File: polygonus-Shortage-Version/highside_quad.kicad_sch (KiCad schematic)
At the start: 11 parts, among them U1102 BTS4175SGA, U1103 BTS4175SGA

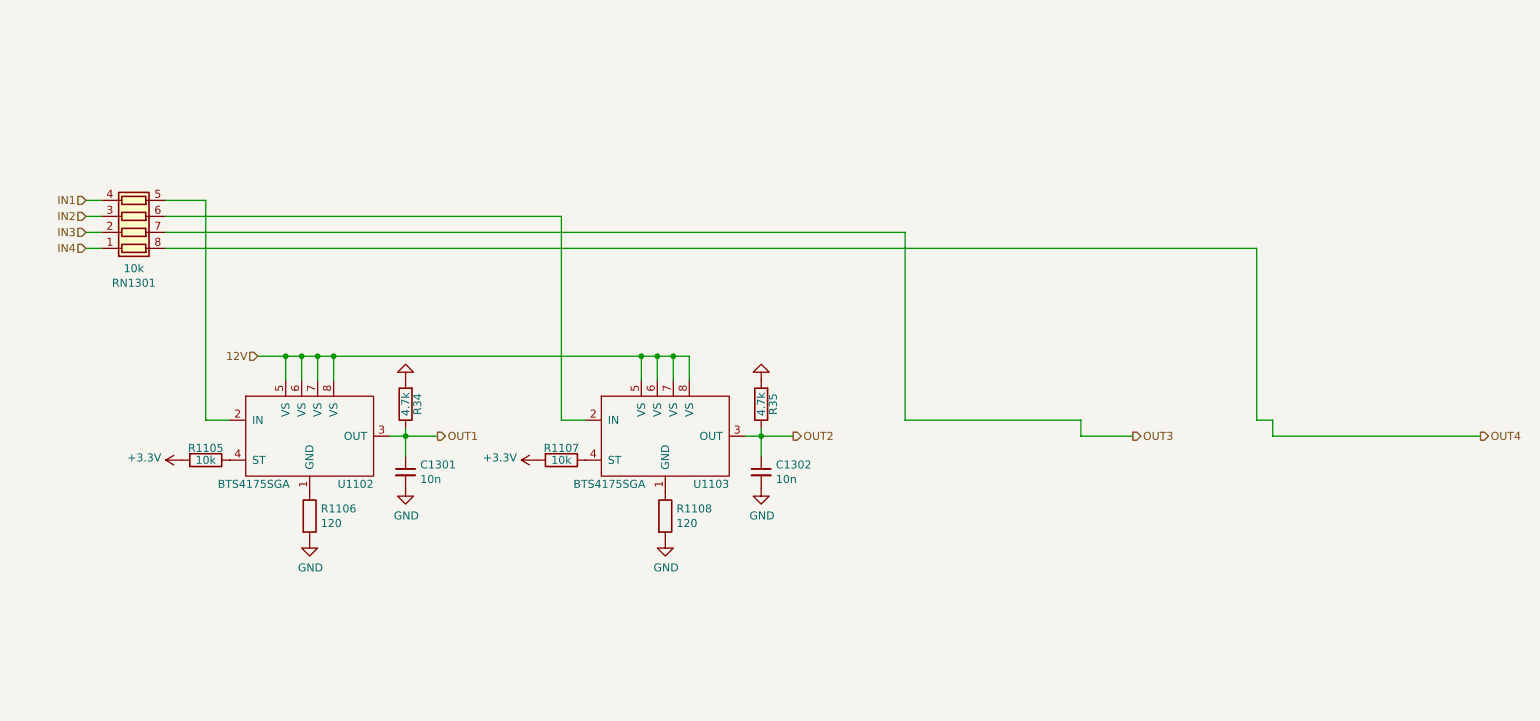
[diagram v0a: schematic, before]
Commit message: Switched highsides, changed TC4427 footprint, swapped USB to other side
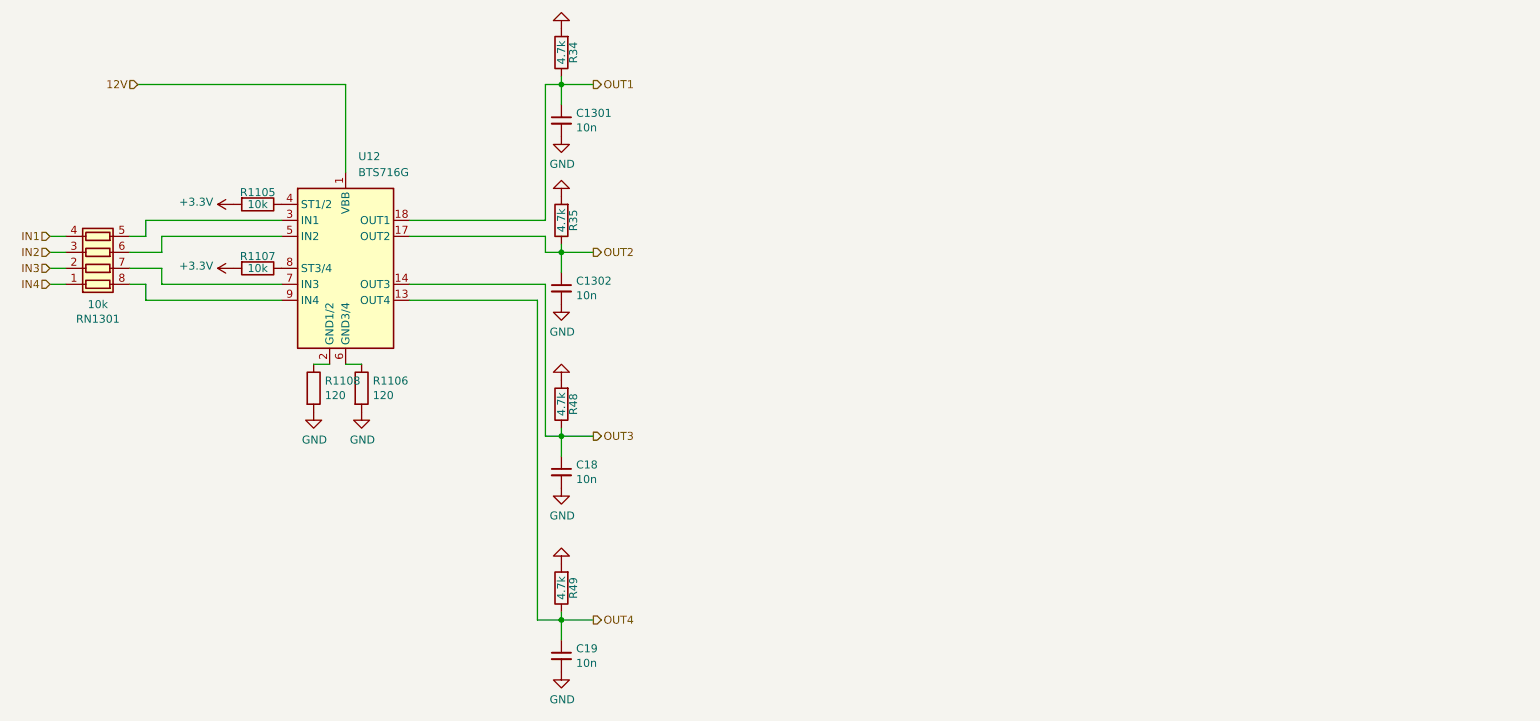
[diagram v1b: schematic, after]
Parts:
- removed U1102, U1103: BTS4175SGA, Package_SO:SOIC-8_3.9x4.9mm_P1.27mm, symbol bts4175:BTS4175SGA
- added C18, C19: 10n, Capacitor_SMD:C_0603_1608Metric, symbol Device:C_Small
- added R48, R49: 4.7k, Resistor_SMD:R_0805_2012Metric, symbol Device:R
- added U12: BTS716G, Package_SO:Infineon_PG-DSO-20-32, symbol Power_Management:BTS716G
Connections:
- net 12V: now also U12.1 (VBB), U12.10 (VBB), U12.11 (VBB), U12.12 (VBB), U12.15 (VBB), U12.16 (VBB), U12.19 (VBB), U12.20 (VBB)
- net GND: now also C18.2, C19.2, R48.2, R49.2
- net OUT1: now also U12.18 (OUT1)
- net OUT2: now also U12.17 (OUT2)
- net OUT3: now also C18.1, R48.1, U12.14 (OUT3); no longer RN1301.7 (R2.2)
- net OUT4: now also C19.1, R49.1, U12.13 (OUT4); no longer RN1301.8 (R1.2)
- net at RN1301.5 (R4.2): now also U12.3 (IN1)
- net at RN1301.6 (R3.2): now also U12.5 (IN2)
- net at R1106.1: now also U12.6 (GND3/4)
- net at R1105.1: now also U12.4 (ST1/2)
- net at R1108.1: now also U12.2 (GND1/2)
- net at R1107.1: now also U12.8 (ST3/4)
- new net: RN1301.7 (R2.2), U12.7 (IN3)
- new net: RN1301.8 (R1.2), U12.9 (IN4)
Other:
- moved on the sheet: C1301, C1302, R1105, R1106, R1107, R1108, R34, R35, RN1301

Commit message: clearout basic version
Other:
- company: rusEFI -> (none)
- title: rusEfi Proteus -> Polygonus
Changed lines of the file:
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@@
   (paper "A4")
   (title_block
-    (title "rusEfi Proteus")
-    (date "2022-04-09")
+    (title "Polygonus")
+    (date "2023-03-15")
     (rev "v0.7")
-    (company "rusEFI")
-    (comment 1 "github.com/mck1117/proteus")
     (comment 2 "rusefi.com/s/proteus")
   )

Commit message: Update to V1.3
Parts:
- renumbered C1301 to C85, C1302 to C86, C18 to C87, C19 to C88, R1107 to R100, R1108 to R101, R1106 to R102, R34 to R103, R35 to R104, R48 to R105, R49 to R106, R1105 to R99, RN1301 to RN11, U12 to U40
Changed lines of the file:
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@@
   (symbol (lib_id "Device:R_Pack04") (at 27.94 68.58 270) (mirror x) (unit 1)
     (in_bom yes) (on_board yes)
-    (property "Reference" "RN1301" (id 0) (at 27.94 79.1718 90))
+    (property "Reference" "RN11" (id 0) (at 27.94 79.1718 90))
     (property "Value" "10k" (id 1) (at 27.94 76.8604 90))
     (property "Footprint" "Resistor_SMD:R_Array_Convex_4x0603" (id 2) (at 27.94 61.595 90)
@@
   (symbol (lib_id "Device:C_Small") (at 101.6 47.625 0) (unit 1)
     (in_bom yes) (on_board yes)
-    (property "Reference" "C1301" (id 0) (at 103.9368 46.4566 0)
+    (property "Reference" "C85" (id 0) (at 103.9368 46.4566 0)
       (effects (font (size 1.27 1.27)) (justify left))
     )
@@
   (symbol (lib_id "Device:C_Small") (at 101.6 74.295 0) (unit 1)
     (in_bom yes) (on_board yes)
-    (property "Reference" "C1302" (id 0) (at 103.9368 73.1266 0)
+    (property "Reference" "C86" (id 0) (at 103.9368 73.1266 0)
       (effects (font (size 1.27 1.27)) (justify left))
     )
@@
   (symbol (lib_id "power:GND") (at 69.85 93.98 0) (unit 1)
     (in_bom yes) (on_board yes)
-    (property "Reference" "#PWR0291" (id 0) (at 69.85 100.33 0)
+    (property "Reference" "#PWR0248" (id 0) (at 69.85 100.33 0)
       (effects (font (size 1.27 1.27)) hide)
     )
@@
   (symbol (lib_id "power:GND") (at 101.6 50.165 0) (unit 1)
     (in_bom yes) (on_board yes)
-    (property "Reference" "#PWR0292" (id 0) (at 101.6 56.515 0)
+    (property "Reference" "#PWR0250" (id 0) (at 101.6 56.515 0)
       (effects (font (size 1.27 1.27)) hide)
     )
@@
   (symbol (lib_id "Device:R") (at 69.85 90.17 0) (unit 1)
     (in_bom yes) (on_board yes)
-    (property "Reference" "R1106" (id 0) (at 71.628 89.0016 0)
+    (property "Reference" "R102" (id 0) (at 71.628 89.0016 0)
       (effects (font (size 1.27 1.27)) (justify left))
     )
@@
   (symbol (lib_id "Device:R") (at 53.34 60.96 270) (unit 1)
     (in_bom yes) (on_board yes)
-    (property "Reference" "R1105" (id 0) (at 53.34 59.055 90))
+    (property "Reference" "R99" (id 0) (at 53.34 59.055 90))
     (property "Value" "10k" (id 1) (at 53.34 60.96 90))
     (property "Footprint" "Resistor_SMD:R_0402_1005Metric" (id 2) (at 53.34 59.182 90)
@@
   (symbol (lib_id "power:+3.3V") (at 49.53 60.96 90) (unit 1)
     (in_bom yes) (on_board yes)
-    (property "Reference" "#PWR0293" (id 0) (at 53.34 60.96 0)
+    (property "Reference" "#PWR0245" (id 0) (at 53.34 60.96 0)
       (effects (font (size 1.27 1.27)) hide)
     )
@@
   (symbol (lib_id "power:GND") (at 62.23 93.98 0) (unit 1)
     (in_bom yes) (on_board yes)
-    (property "Reference" "#PWR0294" (id 0) (at 62.23 100.33 0)
+    (property "Reference" "#PWR0247" (id 0) (at 62.23 100.33 0)
       (effects (font (size 1.27 1.27)) hide)
     )
@@
   (symbol (lib_id "power:GND") (at 101.6 76.835 0) (unit 1)
     (in_bom yes) (on_board yes)
-    (property "Reference" "#PWR0295" (id 0) (at 101.6 83.185 0)
+    (property "Reference" "#PWR0252" (id 0) (at 101.6 83.185 0)
       (effects (font (size 1.27 1.27)) hide)
     )
@@
   (symbol (lib_id "Device:R") (at 62.23 90.17 0) (unit 1)
     (in_bom yes) (on_board yes)
-    (property "Reference" "R1108" (id 0) (at 64.008 89.0016 0)
+    (property "Reference" "R101" (id 0) (at 64.008 89.0016 0)
       (effects (font (size 1.27 1.27)) (justify left))
     )
@@
   (symbol (lib_id "Device:R") (at 53.34 71.12 270) (unit 1)
     (in_bom yes) (on_board yes)
-    (property "Reference" "R1107" (id 0) (at 53.34 69.215 90))
+    (property "Reference" "R100" (id 0) (at 53.34 69.215 90))
     (property "Value" "10k" (id 1) (at 53.34 71.12 90))
     (property "Footprint" "Resistor_SMD:R_0402_1005Metric" (id 2) (at 53.34 69.342 90)
@@
   (symbol (lib_id "power:+3.3V") (at 49.53 71.12 90) (unit 1)
     (in_bom yes) (on_board yes)
-    (property "Reference" "#PWR0296" (id 0) (at 53.34 71.12 0)
+    (property "Reference" "#PWR0246" (id 0) (at 53.34 71.12 0)
       (effects (font (size 1.27 1.27)) hide)
     )
@@
   (symbol (lib_id "Device:R") (at 101.6 36.83 180) (unit 1)
     (in_bom yes) (on_board yes)
-    (property "Reference" "R34" (id 0) (at 103.505 36.83 90))
+    (property "Reference" "R103" (id 0) (at 103.505 36.83 90))
     (property "Value" "4.7k" (id 1) (at 101.6 36.83 90))
     (property "Footprint" "Resistor_SMD:R_0805_2012Metric" (id 2) (at 103.378 36.83 90)
@@
   (symbol (lib_id "power:GND") (at 101.6 33.02 180) (unit 1)
     (in_bom yes) (on_board yes)
-    (property "Reference" "#PWR0120" (id 0) (at 101.6 26.67 0)
+    (property "Reference" "#PWR0249" (id 0) (at 101.6 26.67 0)
       (effects (font (size 1.27 1.27)) hide)
     )
@@
   (symbol (lib_id "Device:R") (at 101.6 63.5 180) (unit 1)
     (in_bom yes) (on_board yes)
-    (property "Reference" "R35" (id 0) (at 103.505 63.5 90))
+    (property "Reference" "R104" (id 0) (at 103.505 63.5 90))
     (property "Value" "4.7k" (id 1) (at 101.6 63.5 90))
     (property "Footprint" "Resistor_SMD:R_0805_2012Metric" (id 2) (at 103.378 63.5 90)
@@
   (symbol (lib_id "power:GND") (at 101.6 59.69 180) (unit 1)
     (in_bom yes) (on_board yes)
-    (property "Reference" "#PWR0121" (id 0) (at 101.6 53.34 0)
+    (property "Reference" "#PWR0251" (id 0) (at 101.6 53.34 0)
       (effects (font (size 1.27 1.27)) hide)
     )
@@
   (symbol (lib_id "power:GND") (at 101.6 118.11 180) (unit 1)
     (in_bom yes) (on_board yes)
-    (property "Reference" "#PWR0155" (id 0) (at 101.6 111.76 0)
+    (property "Reference" "#PWR0255" (id 0) (at 101.6 111.76 0)
       (effects (font (size 1.27 1.27)) hide)
     )
@@
   (symbol (lib_id "Device:R") (at 101.6 121.92 180) (unit 1)
     (in_bom yes) (on_board yes)
-    (property "Reference" "R49" (id 0) (at 103.505 121.92 90))
+    (property "Reference" "R106" (id 0) (at 103.505 121.92 90))
     (property "Value" "4.7k" (id 1) (at 101.6 121.92 90))
     (property "Footprint" "Resistor_SMD:R_0805_2012Metric" (id 2) (at 103.378 121.92 90)
@@
   (symbol (lib_id "Power_Management:BTS716G") (at 67.31 71.12 0) (unit 1)
     (in_bom yes) (on_board yes) (fields_autoplaced)
-    (property "Reference" "U12" (id 0) (at 69.3294 53.34 0)
+    (property "Reference" "U40" (id 0) (at 69.3294 53.34 0)
       (effects (font (size 1.27 1.27)) (justify left))
     )
@@
   (symbol (lib_id "Device:C_Small") (at 101.6 132.715 0) (unit 1)
     (in_bom yes) (on_board yes)
-    (property "Reference" "C19" (id 0) (at 103.9368 131.5466 0)
+    (property "Reference" "C88" (id 0) (at 103.9368 131.5466 0)
       (effects (font (size 1.27 1.27)) (justify left))
     )
@@
   (symbol (lib_id "Device:R") (at 101.6 92.71 180) (unit 1)
     (in_bom yes) (on_board yes)
-    (property "Reference" "R48" (id 0) (at 103.505 92.71 90))
+    (property "Reference" "R105" (id 0) (at 103.505 92.71 90))
     (property "Value" "4.7k" (id 1) (at 101.6 92.71 90))
     (property "Footprint" "Resistor_SMD:R_0805_2012Metric" (id 2) (at 103.378 92.71 90)
@@
   (symbol (lib_id "power:GND") (at 101.6 135.255 0) (unit 1)
     (in_bom yes) (on_board yes)
-    (property "Reference" "#PWR0156" (id 0) (at 101.6 141.605 0)
+    (property "Reference" "#PWR0256" (id 0) (at 101.6 141.605 0)
       (effects (font (size 1.27 1.27)) hide)
     )
@@
   (symbol (lib_id "power:GND") (at 101.6 106.045 0) (unit 1)
     (in_bom yes) (on_board yes)
-    (property "Reference" "#PWR0158" (id 0) (at 101.6 112.395 0)
+    (property "Reference" "#PWR0254" (id 0) (at 101.6 112.395 0)
       (effects (font (size 1.27 1.27)) hide)
     )
@@
   (symbol (lib_id "Device:C_Small") (at 101.6 103.505 0) (unit 1)
     (in_bom yes) (on_board yes)
-    (property "Reference" "C18" (id 0) (at 103.9368 102.3366 0)
+    (property "Reference" "C87" (id 0) (at 103.9368 102.3366 0)
       (effects (font (size 1.27 1.27)) (justify left))
     )
@@
   (symbol (lib_id "power:GND") (at 101.6 88.9 180) (unit 1)
     (in_bom yes) (on_board yes)
-    (property "Reference" "#PWR0157" (id 0) (at 101.6 82.55 0)
-      (effects (font (size 1.27 1.27)) hide)
-    )
+    (property "Reference" "#PWR0253" (id 0) (at 101.6 82.55 0)
+      (effects (font (size 1.27 1.27)) hide)
+    )
